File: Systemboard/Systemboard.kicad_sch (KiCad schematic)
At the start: 17 parts, among them J1 Conn_01x60, J108 Prog BT, U103 ESP32-WROOM-32U

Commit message: user save
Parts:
- removed C1: 0u1, Capacitor_THT:C_Disc_D4.7mm_W2.5mm_P5.00mm, symbol Device:C
- removed C102: 22u, Capacitor_THT:CP_Radial_D5.0mm_P2.00mm, symbol Device:C_Polarized
- removed U103: ESP32-WROOM-32U, RF_Module:ESP32-WROOM-32U, symbol modules:ESP32-WROOM-32U-N16
- added U101: ESP32-WROOM-32E, RF_Module:ESP32-WROOM-32D, symbol RF_Module:ESP32-WROOM-32E
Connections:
- net EN: now also U101.3 (EN)
- net I2S_BCLK: now also U101.11 (IO26)
- net I2S_LRCLK: now also U101.10 (IO25)
- net I2S_SDATA: now also U101.36 (IO22)
- net IO0_BT: now also U101.25 (IO0)
- net RXD_BT: now also U101.34 (RXD0/IO3)
- net TXD_BT: now also U101.35 (TXD0/IO1)
- net USB_SHUNT_SCL: now also U101.13 (IO14)
- net USB_SHUNT_SDA: now also U101.14 (IO12)
- new net: U101.1 (GND), U101.15 (GND), U101.38 (GND), U101.39 (GND)
- no-connect marks 20 -> 4
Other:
- sheet I2S DAC ports: added DAC_OUT_L, DAC_OUT_R; removed +3V3, BT_L, BT_R, ~{DAC_Mute}

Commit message: add I2S MCLK
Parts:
- added R103: 47, Resistor_SMD:R_0402_1005Metric_Pad0.72x0.64mm_HandSolder, symbol Device:R
- R101: value 100E -> 47; footprint Resistor_THT:R_Axial_DIN0207_L6.3mm_D2.5mm_P10.16mm_Horizontal -> Resistor_SMD:R_0402_1005Metric_Pad0.72x0.64mm_HandSolder; DigiKey Part # (none) -> P47DCCT-ND
- R117: footprint Resistor_THT:R_Axial_DIN0207_L6.3mm_D2.5mm_P10.16mm_Horizontal -> Resistor_SMD:R_0402_1005Metric_Pad0.72x0.64mm_HandSolder; DigiKey Part # (none) -> 1276-3431-1-ND
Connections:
- net IO0_BT: now also R103.2
- new net I2S_MCLK: R103.1
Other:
- sheet I2S DAC ports: added I2S_MCLK; removed none
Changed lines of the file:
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@@
 	)
 	(junction
+		(at 138.43 101.6)
+		(diameter 0)
+		(color 0 0 0 0)
+	)
+	(junction
 		(at -58.42 152.4)
 		(diameter 0)
@@
 	(wire
 		(pts
+			(xy 128.27 101.6) (xy 138.43 101.6)
+		)
+		(stroke
+			(width 0)
+			(type default)
+		)
+	)
+	(wire
+		(pts
 			(xy -62.23 101.6) (xy -53.34 101.6)
 		)
@@
 	(wire
 		(pts
+			(xy 138.43 93.98) (xy 138.43 101.6)
+		)
+		(stroke
+			(width 0)
+			(type default)
+		)
+	)
+	(wire
+		(pts
 			(xy -45.72 132.08) (xy -45.72 137.16)
 		)
@@
 	(wire
 		(pts
+			(xy 138.43 101.6) (xy 142.24 101.6)
+		)
+		(stroke
+			(width 0)
+			(type default)
+		)
+	)
+	(wire
+		(pts
 			(xy -53.34 33.02) (xy -45.72 25.4)
 		)
@@
 	(wire
 		(pts
+			(xy 152.4 101.6) (xy 149.86 101.6)
+		)
+		(stroke
+			(width 0)
+			(type default)
+		)
+	)
+	(wire
+		(pts
 			(xy -45.72 48.26) (xy -52.07 41.91)
 		)
@@
 	(global_label "IO0_BT"
 		(shape input)
-		(at 128.27 101.6 0)
+		(at 138.43 93.98 0)
 		(fields_autoplaced yes)
 		(effects
@@
 		)
 		(property "Intersheetrefs" "${INTERSHEET_REFS}"
-			(at 137.5258 101.6 0)
+			(at 147.7652 93.98 0)
 			(effects
 				(font
@@
 		)
 	)
+	(hierarchical_label "I2S_MCLK"
+		(shape input)
+		(at 227.33 113.03 180)
+		(effects
+			(font
+				(size 1.27 1.27)
+			)
+			(justify right)
+		)
+	)
+	(hierarchical_label "I2S_MCLK"
+		(shape output)
+		(at 152.4 101.6 0)
+		(effects
+			(font
+				(size 1.27 1.27)
+			)
+			(justify left)
+		)
+	)
 	(hierarchical_label "I2S_BCLK"
 		(shape output)
@@
 	)
 	(hierarchical_label "I2S_SDATA"
+		(shape input)
+		(at 227.33 120.65 180)
+		(effects
+			(font
+				(size 1.27 1.27)
+			)
+			(justify right)
+		)
+	)
+	(hierarchical_label "I2S_SDATA"
 		(shape output)
 		(at 128.27 139.7 0)
@@
 		)
 	)
+	(hierarchical_label "I2S_BCLK"
+		(shape input)
+		(at 227.33 124.46 180)
+		(effects
+			(font
+				(size 1.27 1.27)
+			)
+			(justify right)
+		)
+	)
 	(hierarchical_label "USB_SHUNT_SCL"
 		(shape input)
@@
 		)
 	)
+	(hierarchical_label "I2S_LRCLK"
+		(shape input)
+		(at 227.33 116.84 180)
+		(effects
+			(font
+				(size 1.27 1.27)
+			)
+			(justify right)
+		)
+	)
 	(symbol
 		(lib_id "mypower:GND")
@@
 	)
 	(symbol
+		(lib_id "Device:R")
+		(at 146.05 101.6 270)
+		(unit 1)
+		(exclude_from_sim no)
+		(in_bom yes)
+		(on_board yes)
+		(dnp no)
+		(property "Reference" "R103"
+			(at 146.05 99.06 90)
+			(effects
+				(font
+					(size 1.27 1.27)
+				)
+			)
+		)
+		(property "Value" "47"
+			(at 146.05 104.14 90)
+			(effects
+				(font
+					(size 1.27 1.27)
+				)
+			)
+		)
+		(property "Footprint" "Resistor_SMD:R_0402_1005Metric_Pad0.72x0.64mm_HandSolder"
+			(at 146.05 99.822 90)
+			(effects
+				(font
+					(size 1.27 1.27)
+				)
+				(hide yes)
+			)
+		)
+		(property "Datasheet" "~"
+			(at 146.05 101.6 0)
+			(effects
+				(font
+					(size 1.27 1.27)
+				)
+				(hide yes)
+			)
+		)
+		(property "Description" ""
+			(at 146.05 101.6 0)
+			(effects
+				(font
+					(size 1.27 1.27)
+				)
+			)
+		)
+		(property "DigiKey Part #" "P47DCCT-ND"
+			(at 146.05 101.6 90)
+			(effects
+				(font
+					(size 1.27 1.27)
+				)
+				(hide yes)
+			)
+		)
+		(pin "1"
+		)
+		(pin "2"
+		)
+		(instances
+			(project "Systemboard"
+				(path "/2f4830bd-672b-4d5b-b8d7-989ae91c893c"
+					(reference "R103")
+					(unit 1)
+				)
+			)
+		)
+	)
+	(symbol
 		(lib_id "power:+3V3")
 		(at 36.83 29.21 0)
@@
 			)
 		)
-		(property "Footprint" "Resistor_THT:R_Axial_DIN0207_L6.3mm_D2.5mm_P10.16mm_Horizontal"
+		(property "Footprint" "Resistor_SMD:R_0402_1005Metric_Pad0.72x0.64mm_HandSolder"
 			(at 75.438 31.75 90)
 			(effects
@@
 			)
 		)
+		(property "DigiKey Part #" "1276-3431-1-ND"
+			(at 73.66 31.75 0)
+			(effects
+				(font
+					(size 1.27 1.27)
+				)
+				(hide yes)
+			)
+		)
 		(pin "1"
 		)
@@
 			)
 		)
-		(property "Value" "100E"
+		(property "Value" "47"
 			(at 85.09 39.37 90)
 			(effects
@@
 			)
 		)
-		(property "Footprint" "Resistor_THT:R_Axial_DIN0207_L6.3mm_D2.5mm_P10.16mm_Horizontal"
+		(property "Footprint" "Resistor_SMD:R_0402_1005Metric_Pad0.72x0.64mm_HandSolder"
 			(at 85.09 35.052 90)
 			(effects
@@
 			)
 		)
+		(property "DigiKey Part #" "P47DCCT-ND"
+			(at 85.09 36.83 90)
+			(effects
+				(font
+					(size 1.27 1.27)
+				)
+				(hide yes)
+			)
+		)
 		(pin "1"
 		)
@@
 		(on_board yes)
 		(dnp no)
-		(fields_autoplaced yes)
 		(property "Reference" "U101"
-			(at 115.1733 93.98 0)
+			(at 114.046 97.79 0)
 			(effects
 				(font
@@
 		)
 		(property "Value" "ESP32-WROOM-32E"
-			(at 115.1733 96.52 0)
+			(at 91.186 97.536 0)
 			(effects
 				(font
@@
 	)
 	(sheet
-		(at 160.274 99.822)
+		(at 227.33 101.854)
 		(size 25.4 25.4)
 		(exclude_from_sim no)
@@
 		)
 		(property "Sheetname" "I2S DAC"
-			(at 160.274 99.1104 0)
+			(at 227.33 101.1424 0)
 			(effects
 				(font
@@
 		)
 		(property "Sheetfile" "I2S_DAC.kicad_sch"
-			(at 160.274 125.8066 0)
+			(at 227.33 127.8386 0)
 			(effects
 				(font
@@
 		)
 		(pin "+5V" input
-			(at 160.274 102.362 180)
+			(at 227.33 104.394 180)
 			(effects
 				(font
@@
 		)
 		(pin "I2S_BCLK" input
-			(at 160.274 122.682 180)
+			(at 227.33 124.46 180)
 			(effects
 				(font
@@
 		)
 		(pin "I2S_LRCLK" input
-			(at 160.274 115.57 180)
+			(at 227.33 116.84 180)
 			(effects
 				(font
@@
 		)
 		(pin "I2S_SDATA" input
-			(at 160.274 119.38 180)
+			(at 227.33 120.65 180)
 			(effects
 				(font
@@
 		)
 		(pin "DAC_OUT_L" output
-			(at 185.674 106.68 0)
+			(at 252.73 108.712 0)
 			(effects
 				(font
@@
 		)
 		(pin "DAC_OUT_R" output
-			(at 185.674 110.49 0)
+			(at 252.73 112.522 0)
 			(effects
 				(font
@@
 			)
 		)
+		(pin "I2S_MCLK" input
+			(at 227.33 113.03 180)
+			(effects
+				(font
+					(size 1.27 1.27)
+				)
+				(justify left)
+			)
+		)

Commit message: user save
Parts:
- removed C117: 1u, Capacitor_THT:CP_Radial_D5.0mm_P2.00mm, symbol Device:C_Polarized
- removed R3, R4: 10k, Resistor_THT:R_Axial_DIN0207_L6.3mm_D2.5mm_P10.16mm_Horizontal, symbol Device:R
- removed R5, R6: 0R, Resistor_THT:R_Axial_DIN0207_L6.3mm_D2.5mm_P10.16mm_Horizontal, symbol Device:R
- removed S1, S2, S3, S4, S5: TL2230EEF100, External_Parts:SW_TL2230EEF100, symbol External_Parts:TL2230EEF100
- added C101: 2u2, Capacitor_SMD:C_0603_1608Metric_Pad1.08x0.95mm_HandSolder, symbol Device:C
- J1: DigiKey Part # (none) -> 900-2004850460CT-ND
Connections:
- net +3V3: now also J1.16 (Pin_16)
- net GND: now also J1.17 (Pin_17), J1.19 (Pin_19), J1.21 (Pin_21), J1.22 (Pin_22), J1.23 (Pin_23), J1.25 (Pin_25), C101.2
- net RCL: now also J1.20 (Pin_20), U101.29 (IO5); no longer J1.41 (Pin_41)
- net SR: now also J1.24 (Pin_24), U101.37 (IO23); no longer J1.37 (Pin_37)
- net SRCL: now also J1.18 (Pin_18), U101.30 (IO18); no longer J1.43 (Pin_43)
- net USB_SHUNT_SCL: now also U101.9 (IO33); no longer U101.13 (IO14)
- net USB_SHUNT_SDA: now also U101.8 (IO32); no longer U101.14 (IO12)
- net Dimmable_V+: now reaches J1.29 (Pin_29)
- net Dimmable_V+: now also J1.26 (Pin_26), J1.27 (Pin_27), J1.28 (Pin_28), J1.30 (Pin_30)
- net at R101.2, R117.1: now also C101.1
- net DAC_CC1: no longer names the net of J1.60 (Pin_60)
- net DAC_CC2: no longer names the net of J1.54 (Pin_54)
- net DAC_D+: no longer names the net of J1.56 (Pin_56)
- net DAC_D-: no longer names the net of J1.57 (Pin_57)
- net DAC_VBUS: no longer names the net of J1.59 (Pin_59)
- removed net GNDD: J1.36 (Pin_36), J1.38 (Pin_38), J1.40 (Pin_40), J1.42 (Pin_42), J1.44 (Pin_44), J1.46 (Pin_46), J1.49 (Pin_49), J1.55 (Pin_55), J1.58 (Pin_58)
- net SRCR: no longer names the net of J1.45 (Pin_45)
- removed net VCC: J1.31 (Pin_31), J1.32 (Pin_32), J1.33 (Pin_33), J1.34 (Pin_34), J1.35 (Pin_35)
- net ~{OE}: no longer names the net of J1.39 (Pin_39)
- no-connect marks 4 -> 2
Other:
- note removed: "https://www.digikey.at/de/products/detail/espressif-systems/ESP32-WROOM-32E-N16/11613144"
- note removed: "https://www.digikey.at/de/products/detail/texas-instruments/INA226AIDGSR/2687236"
- moved on the sheet: J1, J108, R101, R103, R117, U101

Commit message: Update Systemboard.kicad_sch
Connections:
- net CHARGER_VBUS: now also J1.10 (Pin_10), J1.9 (Pin_9)
- net GND: now also J1.12 (Pin_12), J1.15 (Pin_15), J1.3 (Pin_3), J1.6 (Pin_6)
- net DAC_CC1: now reaches J1.1 (Pin_1)
- net CHARGER_CC2: now reaches J1.11 (Pin_11)
- net CHARGER_D+: now reaches J1.13 (Pin_13)
- net CHARGER_D-: now reaches J1.14 (Pin_14)
- net DAC_VBUS: now reaches J1.2 (Pin_2)
- net BTN_5_NC_B: now reaches J1.31 (Pin_31)
- net BTN_5_NC_A: now reaches J1.32 (Pin_32)
- net BTN_5_COM_B: now reaches J1.33 (Pin_33)
- net BTN_5_COM_A: now reaches J1.34 (Pin_34)
- net BTN_5_NO_B: now reaches J1.35 (Pin_35)
- net BTN_5_NO_A: now reaches J1.36 (Pin_36)
- net BTN_4_NC_B: now reaches J1.37 (Pin_37)
- net BTN_4_NC_A: now reaches J1.38 (Pin_38)
- net BTN_4_COM_B: now reaches J1.39 (Pin_39)
- net DAC_D-: now reaches J1.4 (Pin_4)
- net BTN_4_COM_A: now reaches J1.40 (Pin_40)
- net BTN_4_NO_B: now reaches J1.41 (Pin_41)
- net BTN_4_NO_A: now reaches J1.42 (Pin_42)
- net BTN_3_NO_B: now reaches J1.43 (Pin_43)
- net BTN_3_NO_A: now reaches J1.44 (Pin_44)
- net BTN_3_COM_B: now reaches J1.45 (Pin_45)
- net BTN_3_COM_A: now reaches J1.46 (Pin_46)
- net BTN_3_NC_B: now reaches J1.47 (Pin_47)
- net BTN_3_NC_A: now reaches J1.48 (Pin_48)
- net BTN_2_NC_B: now reaches J1.49 (Pin_49)
- net DAC_D+: now reaches J1.5 (Pin_5)
- net BTN_2_NC_A: now reaches J1.50 (Pin_50)
- net BTN_2_COM_B: now reaches J1.51 (Pin_51)
- net BTN_2_COM_A: now reaches J1.52 (Pin_52)
- net BTN_2_NO_B: now reaches J1.53 (Pin_53)
- net BTN_2_NO_A: now reaches J1.54 (Pin_54)
- net BTN_1_NO_B: now reaches J1.55 (Pin_55)
- net BTN_1_NO_A: now reaches J1.56 (Pin_56)
- net BTN_1_COM_B: now reaches J1.57 (Pin_57)
- net BTN_1_COM_A: now reaches J1.58 (Pin_58)
- net BTN_1_NC_B: now reaches J1.59 (Pin_59)
- net BTN_1_NC_A: now reaches J1.60 (Pin_60)
- net DAC_CC2: now reaches J1.7 (Pin_7)
- net CHARGER_CC1: now reaches J1.8 (Pin_8)

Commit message: Update Systemboard.kicad_sch
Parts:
- added C102, C103, C104, C105, C106: 100n, Capacitor_SMD:C_0805_2012Metric_Pad1.18x1.45mm_HandSolder, symbol Device:C
- added R102, R106, R108, R110, R112: 47, Resistor_SMD:R_0402_1005Metric_Pad0.72x0.64mm_HandSolder, symbol Device:R
- added R104, R105, R107, R109, R111, R113: 10k, Resistor_SMD:R_0402_1005Metric_Pad0.72x0.64mm_HandSolder, symbol Device:R
- added U102: 74HC14, Package_SO:SOIC-14_3.9x8.7mm_P1.27mm, symbol 74xx:74HC14
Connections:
- net +3V3: now also R104.2, R105.2, R107.2, R109.2, R111.2
- net GND: now also C102.2, C103.2, C104.2, C105.2, C106.2, R113.1
- new net: C106.1, R111.1, R112.2, U102.11
- new net: C103.1, R105.1, R106.2, U102.3
- new net: C105.1, R109.1, R110.2, U102.9
- new net: C104.1, R107.1, R108.2, U102.5
- new net: C102.1, R102.2, R104.1, U102.1
- new net: R113.2, U102.13
- no-connect marks 2 -> 3
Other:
- note added: "check whether the headset uses NC or NO switches and reserve that switches for them"
- moved on the sheet: R103, U101

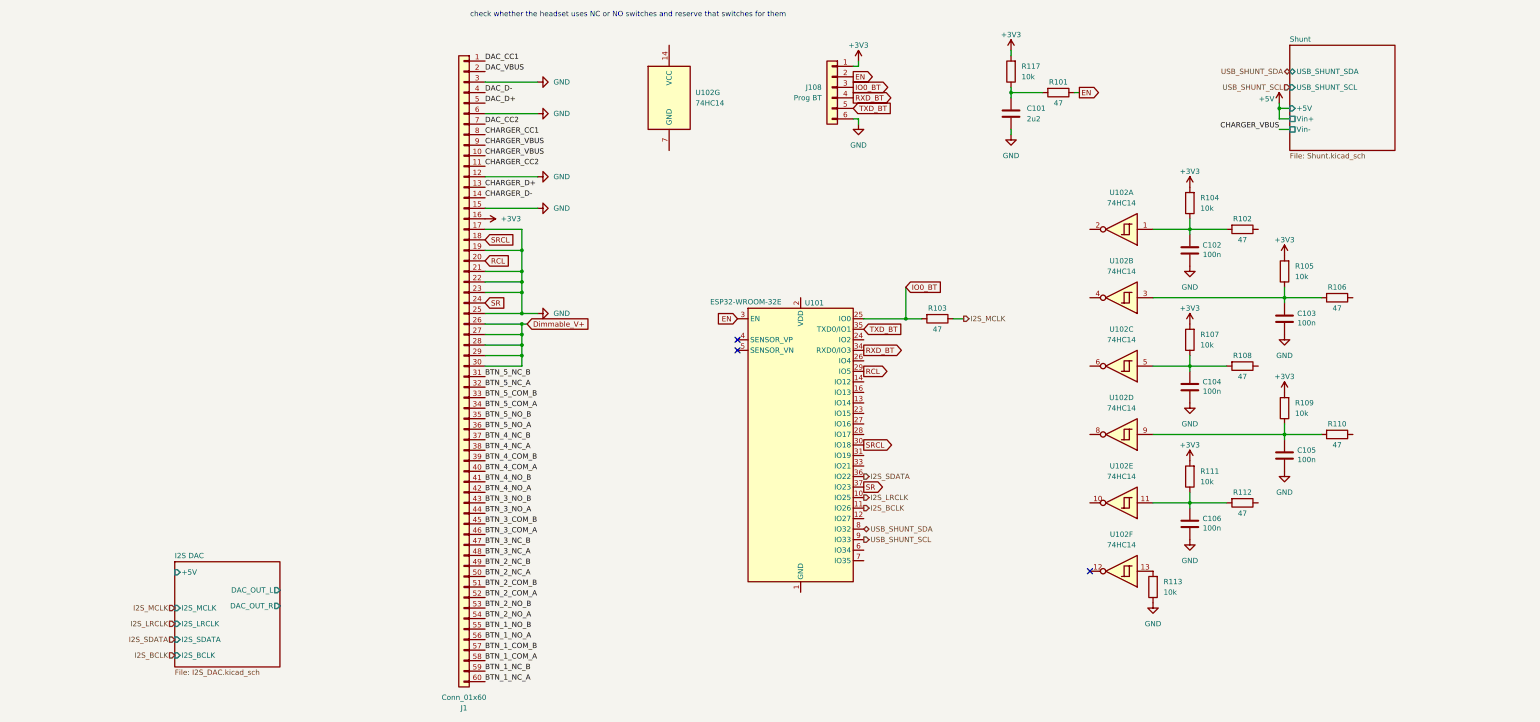
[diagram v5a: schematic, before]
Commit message: Add debouncer schematic to Systemboard
Added Debouncer.kicad_sch schematic for the Systemboard, updated .gitignore to exclude fp-info-cache, and made related project and schematic updates. This introduces a debouncer circuit using a 74HC14 Schmitt trigger and associated passive components.
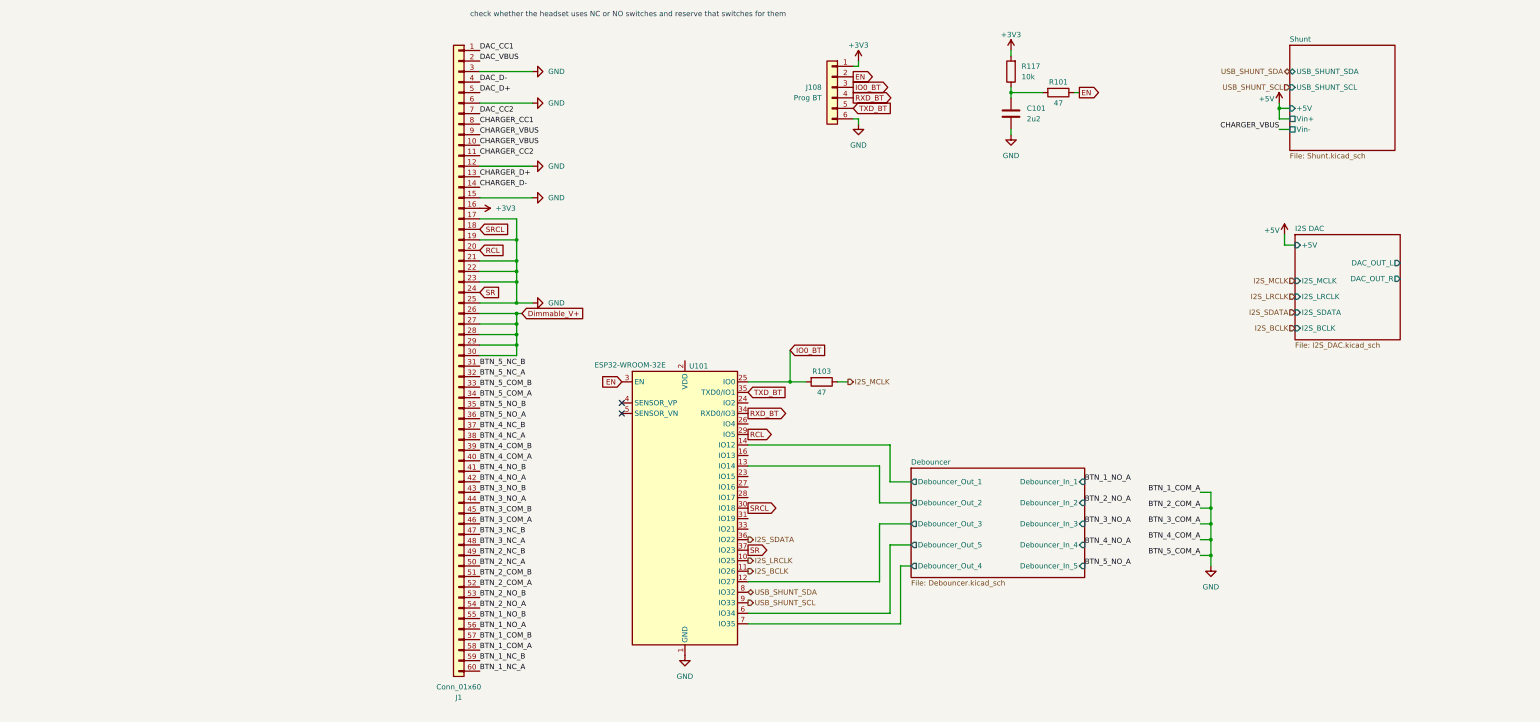
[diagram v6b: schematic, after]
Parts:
- removed C102, C103, C104, C105, C106: 100n, Capacitor_SMD:C_0805_2012Metric_Pad1.18x1.45mm_HandSolder, symbol Device:C
- removed R102, R106, R108, R110, R112: 47, Resistor_SMD:R_0402_1005Metric_Pad0.72x0.64mm_HandSolder, symbol Device:R
- removed R104, R105, R107, R109, R111, R113: 10k, Resistor_SMD:R_0402_1005Metric_Pad0.72x0.64mm_HandSolder, symbol Device:R
- removed U102: 74HC14, Package_SO:SOIC-14_3.9x8.7mm_P1.27mm, symbol 74xx:74HC14
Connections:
- net BTN_1_COM_A is gone; now on net GND: J1.58 (Pin_58)
- net BTN_2_COM_A is gone; now on net GND: J1.52 (Pin_52)
- net BTN_3_COM_A is gone; now on net GND: J1.46 (Pin_46)
- net BTN_4_COM_A is gone; now on net GND: J1.40 (Pin_40)
- net BTN_5_COM_A is gone; now on net GND: J1.34 (Pin_34)
- net GND: now also U101.1 (GND), U101.15 (GND), U101.38 (GND), U101.39 (GND)
- net Debouncer/Debouncer_Out_3: now reaches U101.12 (IO27)
- net Debouncer/Debouncer_Out_2: now reaches U101.13 (IO14)
- net Debouncer/Debouncer_Out_1: now reaches U101.14 (IO12)
- net Debouncer/Debouncer_Out_5: now reaches U101.6 (IO34)
- net Debouncer/Debouncer_Out_4: now reaches U101.7 (IO35)
- no-connect marks 3 -> 2
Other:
- added sheet Debouncer (Debouncer.kicad_sch)
- moved on the sheet: J1, R103, U101

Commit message: Update Systemboard.kicad_sch
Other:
- note added: "check whether the headset uses NC or NO switches and reserve that switches for them amplifier power supply high-current 5V, +/-12V maybe, high-current dimmable 2V-3V3 reed switches"
- note removed: "check whether the headset uses NC or NO switches and reserve that switches for them"
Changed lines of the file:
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@@
 	(generator_version "9.0")
 	(paper "A4")
-	(text "check whether the headset uses NC or NO switches and reserve that switches for them"
+	(text "check whether the headset uses NC or NO switches and reserve that switches for them\n\namplifier\n\npower supply\nhigh-current 5V, +/-12V maybe, high-current dimmable 2V-3V3\n\nreed switches"
 		(exclude_from_sim no)
-		(at 67.564 18.034 0)
+		(at 114.3 65.278 0)
 		(effects
 			(font

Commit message: start amplifier design
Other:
- added sheet Amplifier (Amplifier.kicad_sch)
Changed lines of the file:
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@@
+		)
+	)
+	(sheet
+		(at 228.854 127)
+		(size 25.4 25.908)
+		(exclude_from_sim no)
+		(in_bom yes)
+		(on_board yes)
+		(dnp no)
+		(fields_autoplaced yes)
+		(stroke
+			(width 0.1524)
+			(type solid)
+		)
+		(fill
+			(color 0 0 0 0.0000)
+		)
+		(property "Sheetname" "Amplifier"
+			(at 228.854 126.2884 0)
+			(effects
+				(font
+					(size 1.27 1.27)
+				)
+				(justify left bottom)
+			)
+		)
+		(property "Sheetfile" "Amplifier.kicad_sch"
+			(at 228.854 153.4926 0)
+			(effects
+				(font
+					(size 1.27 1.27)
+				)
+				(justify left top)
+			)
+		)
+		(instances
+			(project "Systemboard"
+				(path "/2f4830bd-672b-4d5b-b8d7-989ae91c893c"
+					(page "5")
+				)
+			)
 		)
 	)
